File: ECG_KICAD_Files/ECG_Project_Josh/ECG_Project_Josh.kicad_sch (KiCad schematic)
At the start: 35 parts, among them J1 Conn_01x02_Pin, J2 Conn_01x02_Pin, J3 Conn_01x03_Pin, U1 LF412ACN/NOPB, U2 AD623AN, U3 LF412ACN/NOPB

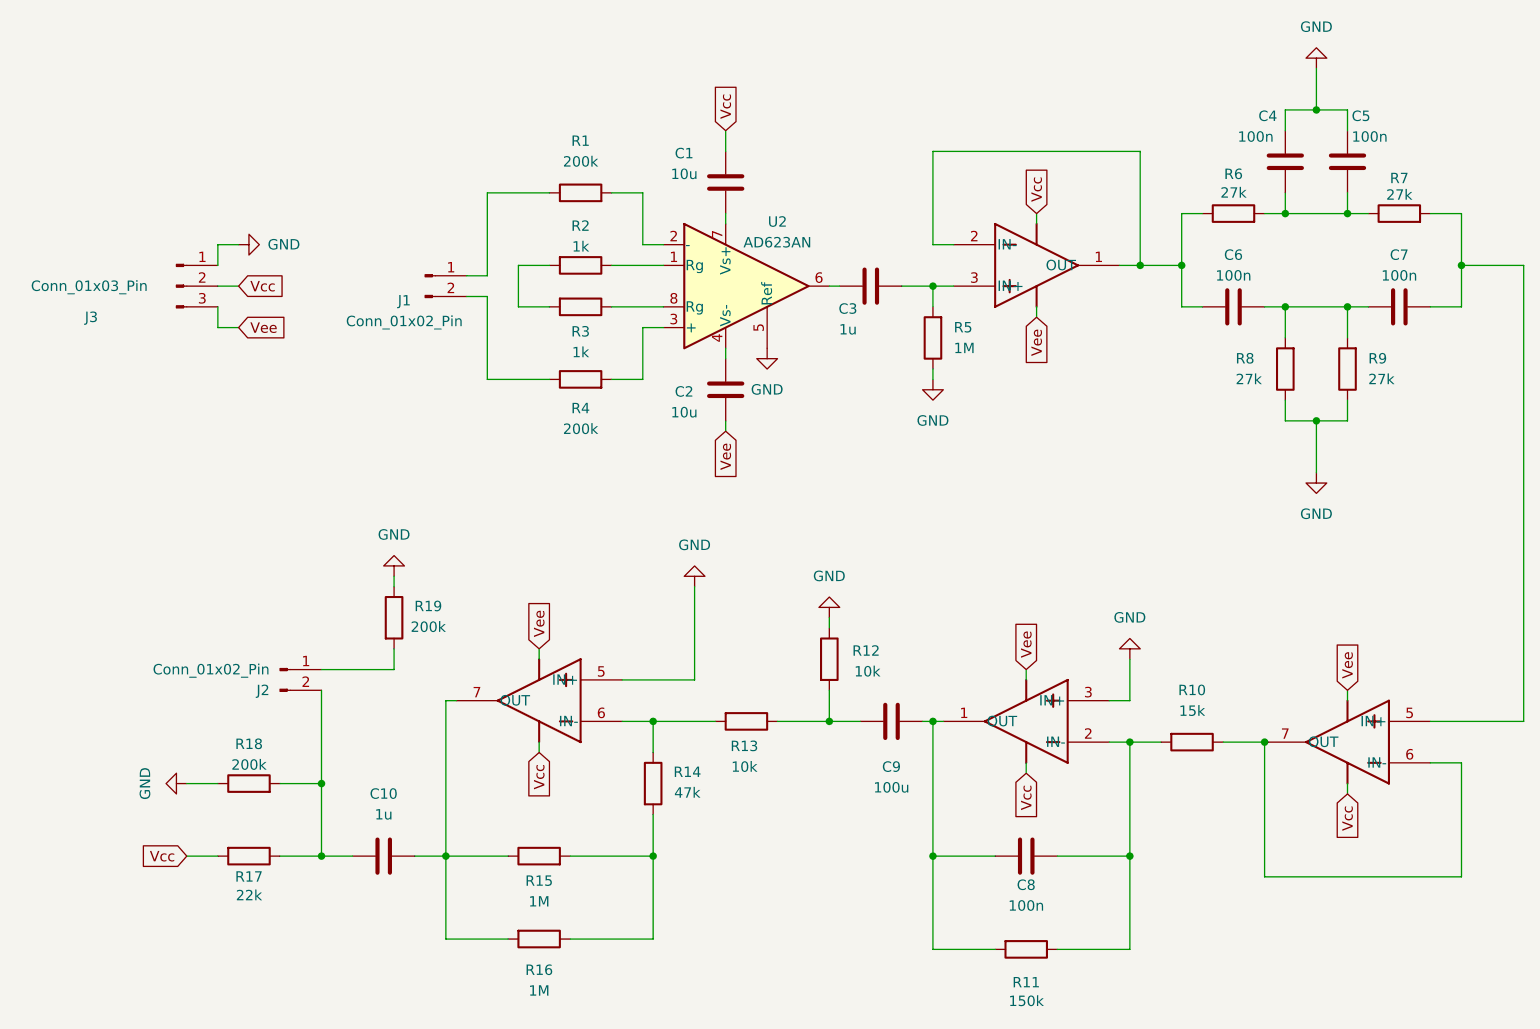
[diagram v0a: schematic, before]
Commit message: pin update for symbol
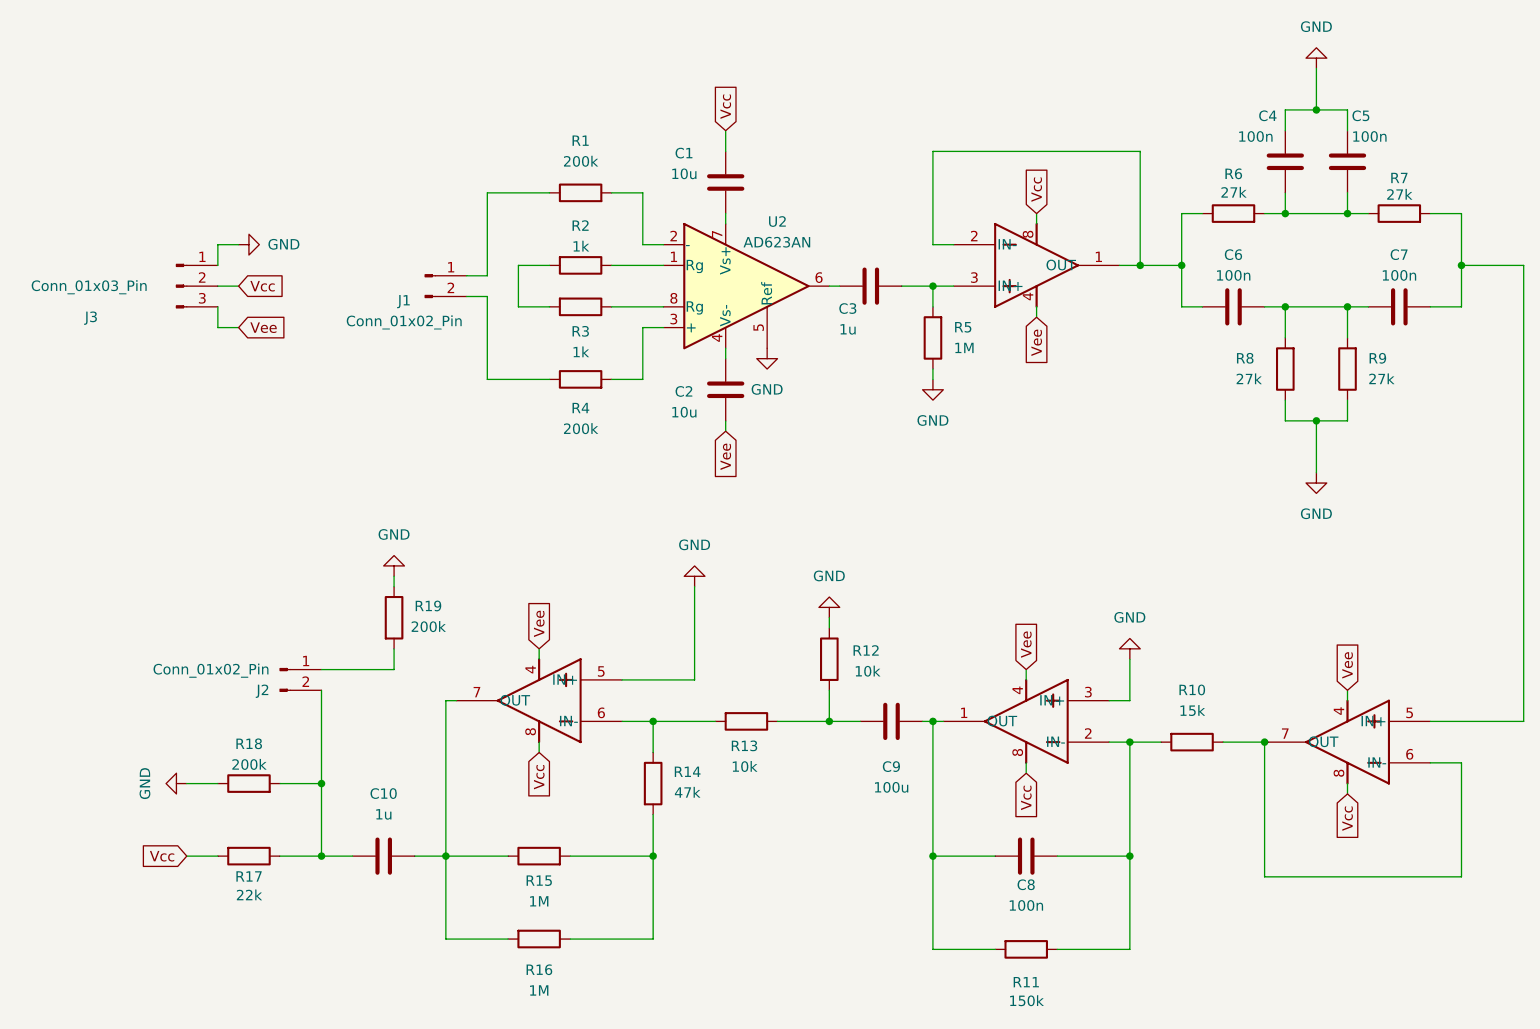
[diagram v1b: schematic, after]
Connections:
- net Vcc: now also U1.8, U1.8, U3.8, U3.8
- net Vee: now also U1.4, U1.4, U3.4, U3.4
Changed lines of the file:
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@@
 		(pin "7"
+		)
+		(pin "8"
+		)
+		(pin "4"
+		)
+		(pin "8"
+		)
+		(pin "4"
 		)
 		(instances
@@
 		(pin "1"
 		)
+		(pin "4"
+		)
+		(pin "8"
+		)
+		(pin "4"
+		)
+		(pin "8"
+		)
 		(instances
 			(project ""
@@
 	)
 	(symbol
+		(lib_name "LF412ACN_NOPB_1")
 		(lib_id "2026-02-26_19-36-44:LF412ACN_NOPB")
 		(at 209.55 125.73 180)
@@
 		(pin "7"
 		)
+		(pin "8"
+		)
+		(pin "4"
+		)
+		(pin "4"
+		)
+		(pin "8"
+		)
 		(instances
 			(project ""
@@
 	)
 	(symbol
+		(lib_name "LF412ACN_NOPB_2")
 		(lib_id "2026-02-26_19-47-40:LF412ACN_NOPB")
 		(at 170.18 123.19 180)
@@
 		(pin "1"
 		)
-		(instances
+		(pin "8"
+		)
+		(pin "4"
+		)
+		(pin "4"
+		)
+		(pin "8"
+		)
+		(instances

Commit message: PCB Complete DRM Passed
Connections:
- net Vcc: now also J3.3 (Pin_3); no longer J3.2 (Pin_2)
- net Vee: now also J3.2 (Pin_2); no longer J3.3 (Pin_3)
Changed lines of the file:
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@@
 	(wire
 		(pts
-			(xy 68.58 69.85) (xy 66.04 69.85)
+			(xy 68.58 71.12) (xy 66.04 71.12)
 		)
 		(stroke
@@
 	(wire
 		(pts
-			(xy 66.04 69.85) (xy 66.04 67.31)
+			(xy 66.04 71.12) (xy 66.04 67.31)
 		)
 		(stroke
@@
 		)
 	)
+	(global_label "Vee"
+		(shape input)
+		(at 166.37 68.58 270)
+		(fields_autoplaced yes)
+		(effects
+			(font
+				(size 1.27 1.27)
+			)
+			(justify right)
+		)
+		(property "Intersheetrefs" "${INTERSHEET_REFS}"
+			(at 166.37 74.831 90)
+			(effects
+				(font
+					(size 1.27 1.27)
+				)
+				(justify right)
+				(hide yes)
+			)
+		)
+	)
 	(global_label "Vcc"
 		(shape input)
+		(at 204.47 127 270)
+		(fields_autoplaced yes)
+		(effects
+			(font
+				(size 1.27 1.27)
+			)
+			(justify right)
+		)
+		(property "Intersheetrefs" "${INTERSHEET_REFS}"
+			(at 204.47 133.251 90)
+			(effects
+				(font
+					(size 1.27 1.27)
+				)
+				(justify right)
+				(hide yes)
+			)
+		)
+	)
+	(global_label "Vee"
+		(shape input)
+		(at 105.41 109.22 90)
+		(fields_autoplaced yes)
+		(effects
+			(font
+				(size 1.27 1.27)
+			)
+			(justify left)
+		)
+		(property "Intersheetrefs" "${INTERSHEET_REFS}"
+			(at 105.41 102.969 90)
+			(effects
+				(font
+					(size 1.27 1.27)
+				)
+				(justify left)
+				(hide yes)
+			)
+		)
+	)
+	(global_label "Vcc"
+		(shape input)
+		(at 166.37 55.88 90)
+		(fields_autoplaced yes)
+		(effects
+			(font
+				(size 1.27 1.27)
+			)
+			(justify left)
+		)
+		(property "Intersheetrefs" "${INTERSHEET_REFS}"
+			(at 166.37 49.629 90)
+			(effects
+				(font
+					(size 1.27 1.27)
+				)
+				(justify left)
+				(hide yes)
+			)
+		)
+	)
+	(global_label "Vcc"
+		(shape input)
+		(at 68.58 71.12 0)
+		(fields_autoplaced yes)
+		(effects
+			(font
+				(size 1.27 1.27)
+			)
+			(justify left)
+		)
+		(property "Intersheetrefs" "${INTERSHEET_REFS}"
+			(at 74.831 71.12 0)
+			(effects
+				(font
+					(size 1.27 1.27)
+				)
+				(justify left)
+				(hide yes)
+			)
+		)
+	)
+	(global_label "Vee"
+		(shape input)
+		(at 165.1 111.76 90)
+		(fields_autoplaced yes)
+		(effects
+			(font
+				(size 1.27 1.27)
+			)
+			(justify left)
+		)
+		(property "Intersheetrefs" "${INTERSHEET_REFS}"
+			(at 165.1 105.509 90)
+			(effects
+				(font
+					(size 1.27 1.27)
+				)
+				(justify left)
+				(hide yes)
+			)
+		)
+	)
+	(global_label "Vcc"
+		(shape input)
+		(at 165.1 124.46 270)
+		(fields_autoplaced yes)
+		(effects
+			(font
+				(size 1.27 1.27)
+			)
+			(justify right)
+		)
+		(property "Intersheetrefs" "${INTERSHEET_REFS}"
+			(at 165.1 130.711 90)
+			(effects
+				(font
+					(size 1.27 1.27)
+				)
+				(justify right)
+				(hide yes)
+			)
+		)
+	)
+	(global_label "Vcc"
+		(shape input)
+		(at 105.41 121.92 270)
+		(fields_autoplaced yes)
+		(effects
+			(font
+				(size 1.27 1.27)
+			)
+			(justify right)
+		)
+		(property "Intersheetrefs" "${INTERSHEET_REFS}"
+			(at 105.41 128.171 90)
+			(effects
+				(font
+					(size 1.27 1.27)
+				)
+				(justify right)
+				(hide yes)
+			)
+		)
+	)
+	(global_label "Vee"
+		(shape input)
 		(at 68.58 64.77 0)
 		(fields_autoplaced yes)
@@
 				(hide yes)
 			)
-		)
-	)
-	(global_label "Vee"
-		(shape input)
-		(at 166.37 68.58 270)
-		(fields_autoplaced yes)
-		(effects
-			(font
-				(size 1.27 1.27)
-			)
-			(justify right)
-		)
-		(property "Intersheetrefs" "${INTERSHEET_REFS}"
-			(at 166.37 74.831 90)
-			(effects
-				(font
-					(size 1.27 1.27)
-				)
-				(justify right)
-				(hide yes)
-			)
-		)
-	)
-	(global_label "Vee"
-		(shape input)
-		(at 68.58 69.85 0)
-		(fields_autoplaced yes)
-		(effects
-			(font
-				(size 1.27 1.27)
-			)
-			(justify left)
-		)
-		(property "Intersheetrefs" "${INTERSHEET_REFS}"
-			(at 74.831 69.85 0)
-			(effects
-				(font
-					(size 1.27 1.27)
-				)
-				(justify left)
-				(hide yes)
-			)
-		)
-	)
-	(global_label "Vcc"
-		(shape input)
-		(at 204.47 127 270)
-		(fields_autoplaced yes)
-		(effects
-			(font
-				(size 1.27 1.27)
-			)
-			(justify right)
-		)
-		(property "Intersheetrefs" "${INTERSHEET_REFS}"
-			(at 204.47 133.251 90)
-			(effects
-				(font
-					(size 1.27 1.27)
-				)
-				(justify right)
-				(hide yes)
-			)
-		)
-	)
-	(global_label "Vee"
-		(shape input)
-		(at 105.41 109.22 90)
-		(fields_autoplaced yes)
-		(effects
-			(font
-				(size 1.27 1.27)
-			)
-			(justify left)
-		)
-		(property "Intersheetrefs" "${INTERSHEET_REFS}"
-			(at 105.41 102.969 90)
-			(effects
-				(font
-					(size 1.27 1.27)
-				)
-				(justify left)
-				(hide yes)
-			)
-		)
-	)
-	(global_label "Vcc"
-		(shape input)
-		(at 166.37 55.88 90)
-		(fields_autoplaced yes)
-		(effects
-			(font
-				(size 1.27 1.27)
-			)
-			(justify left)
-		)
-		(property "Intersheetrefs" "${INTERSHEET_REFS}"
-			(at 166.37 49.629 90)
-			(effects
-				(font
-					(size 1.27 1.27)
-				)
-				(justify left)
-				(hide yes)
-			)
-		)
-	)
-	(global_label "Vee"
-		(shape input)
-		(at 165.1 111.76 90)
-		(fields_autoplaced yes)
-		(effects
-			(font
-				(size 1.27 1.27)
-			)
-			(justify left)
-		)
-		(property "Intersheetrefs" "${INTERSHEET_REFS}"
-			(at 165.1 105.509 90)
-			(effects
-				(font
-					(size 1.27 1.27)
-				)
-				(justify left)
-				(hide yes)
-			)
-		)
-	)
-	(global_label "Vcc"
-		(shape input)
-		(at 165.1 124.46 270)
-		(fields_autoplaced yes)
-		(effects
-			(font
-				(size 1.27 1.27)
-			)
-			(justify right)
-		)
-		(property "Intersheetrefs" "${INTERSHEET_REFS}"
-			(at 165.1 130.711 90)
-			(effects
-				(font
-					(size 1.27 1.27)
-				)
-				(justify right)
-				(hide yes)
-			)
-		)
-	)
-	(global_label "Vcc"
-		(shape input)
-		(at 105.41 121.92 270)
-		(fields_autoplaced yes)
-		(effects
-			(font
-				(size 1.27 1.27)
-			)
-			(justify right)
-		)
-		(property "Intersheetrefs" "${INTERSHEET_REFS}"
-			(at 105.41 128.171 90)
-			(effects
-				(font
-					(size 1.27 1.27)
-				)
-				(justify right)
-				(hide yes)
-			)
